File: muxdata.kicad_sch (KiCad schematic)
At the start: 5 parts, among them U22 XC4003-VQ100, U3 74LS245, U4 74LS245, U5 74LS245, U6 74LS245

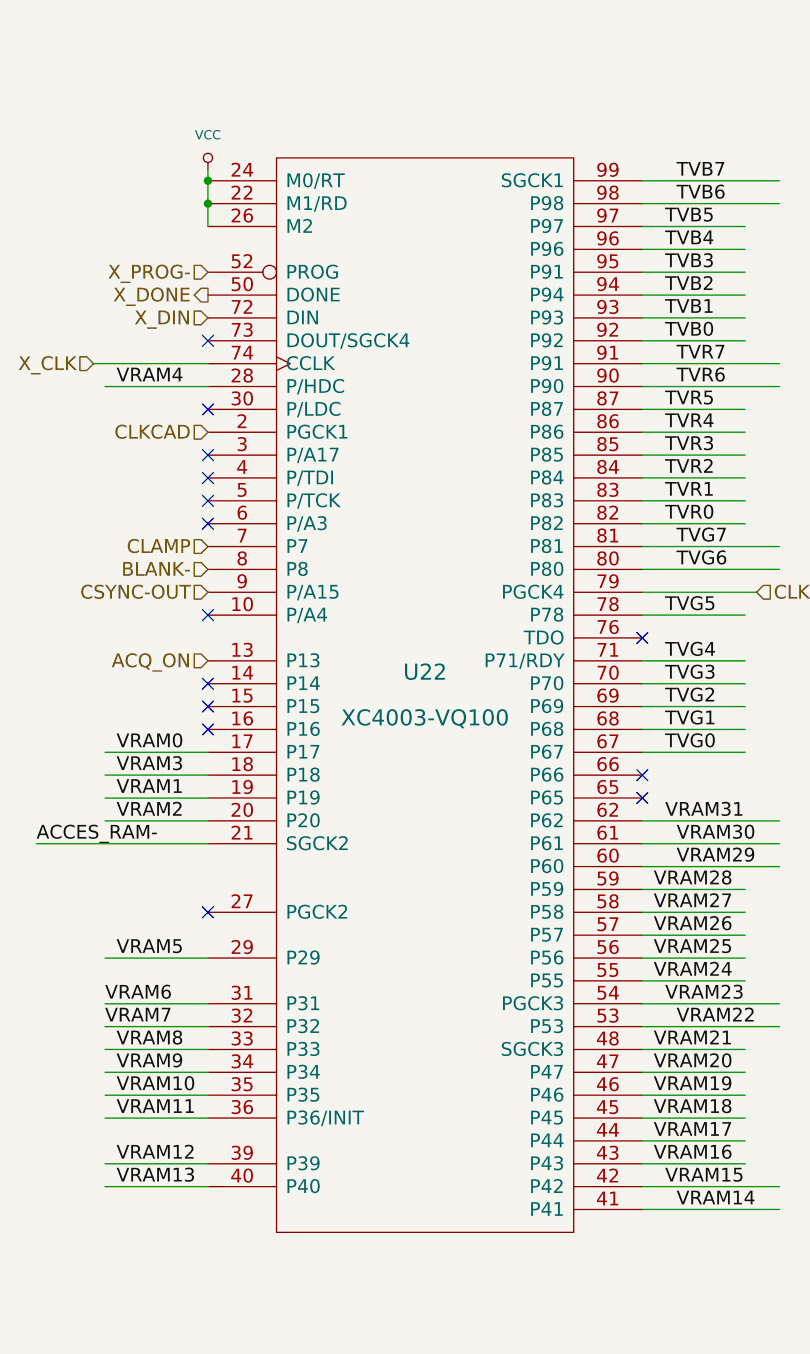
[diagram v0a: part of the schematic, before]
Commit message: update to kicad 9
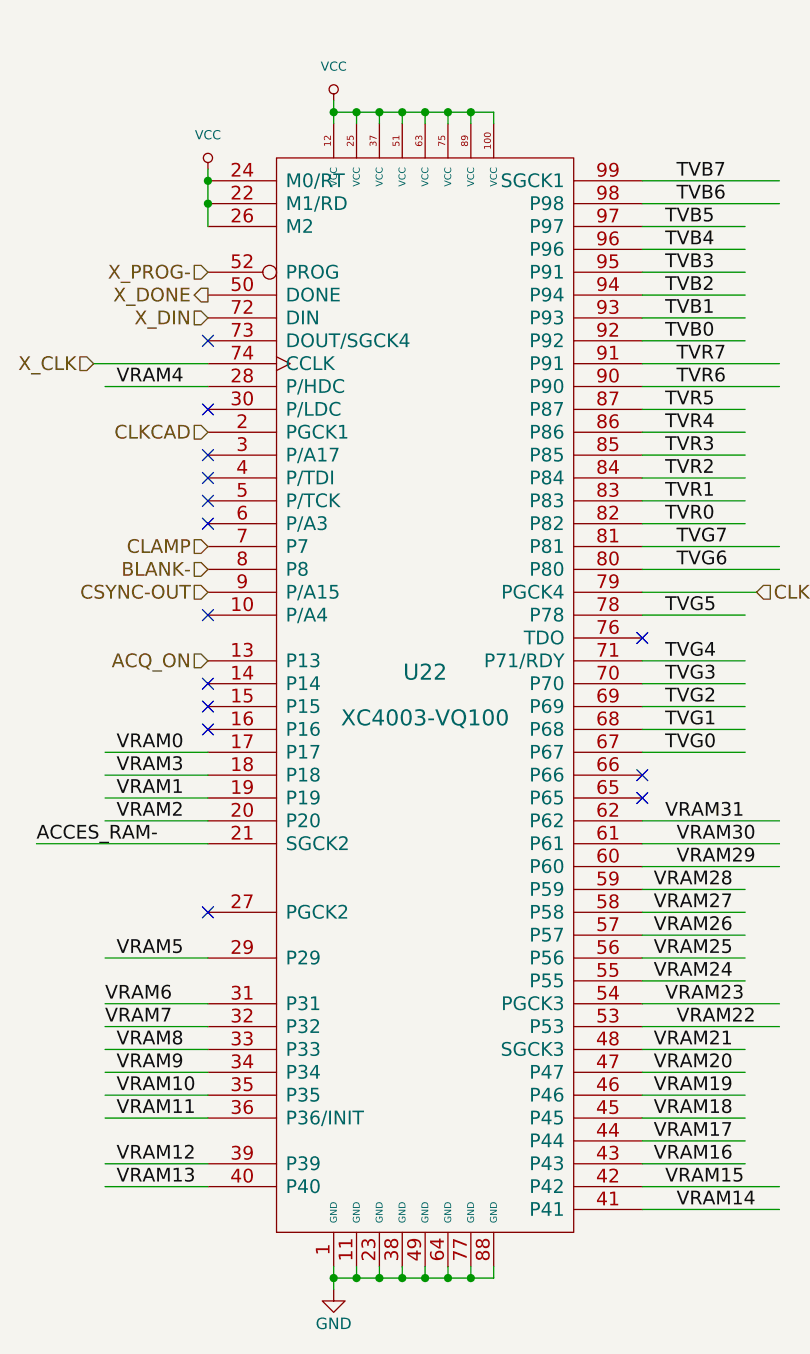
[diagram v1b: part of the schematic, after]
